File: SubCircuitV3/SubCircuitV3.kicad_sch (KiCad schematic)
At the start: 49 parts, among them J1 JTAG, J10 ESC_POWER, J11 ESC_POWER, J12 ESC_POWER, J13 ESC_POWER, J14 FEMALE XT-60, J15 ESC PWM, J16 5S, J17 Water Sensor Input, J18 3S OUT, J19 2S OUT, J2 ESC PWM, J20 SWITCH, J21 U3V16F15, J22 CAM OUT, J3 ESC PWM, J4 ESC PWM, J5 ESC PWM, J6 ESC PWM, J7 3S, J8 ESC_POWER, J9 ESC_POWER, K1 G5Q-1A, Q1 NMOS, Q2 NMOS, Q3 NMOS, Q4 NMOS, Q5 NMOS, Q6 NMOS

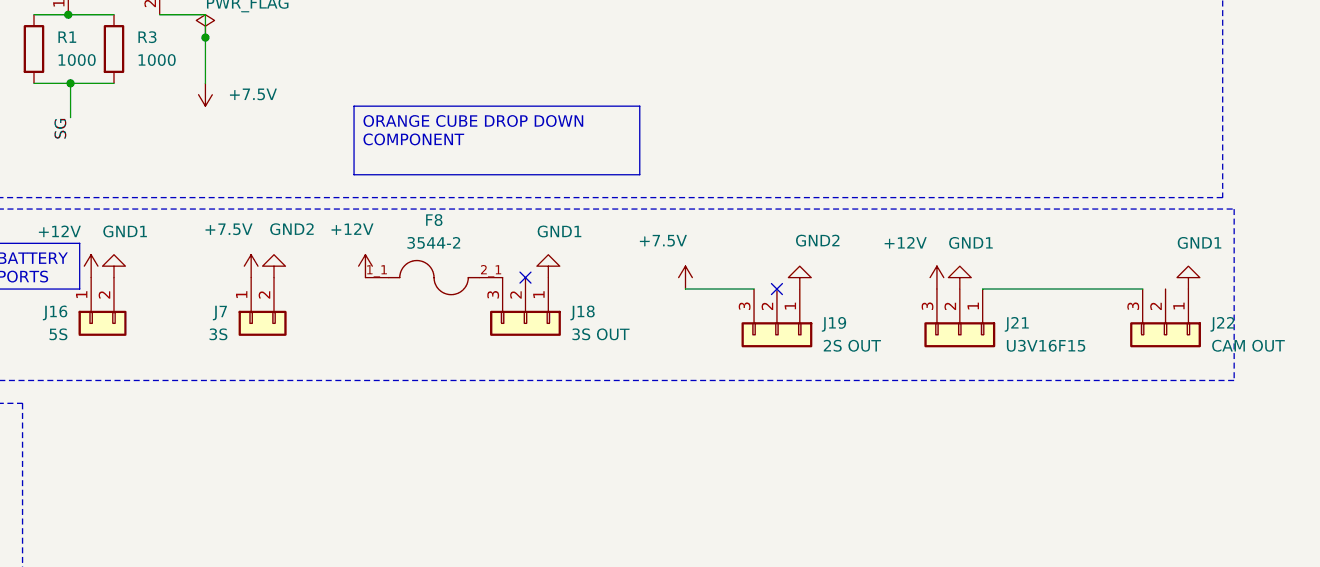
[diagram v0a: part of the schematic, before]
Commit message: Replaced old boost convertor with U3V70F15
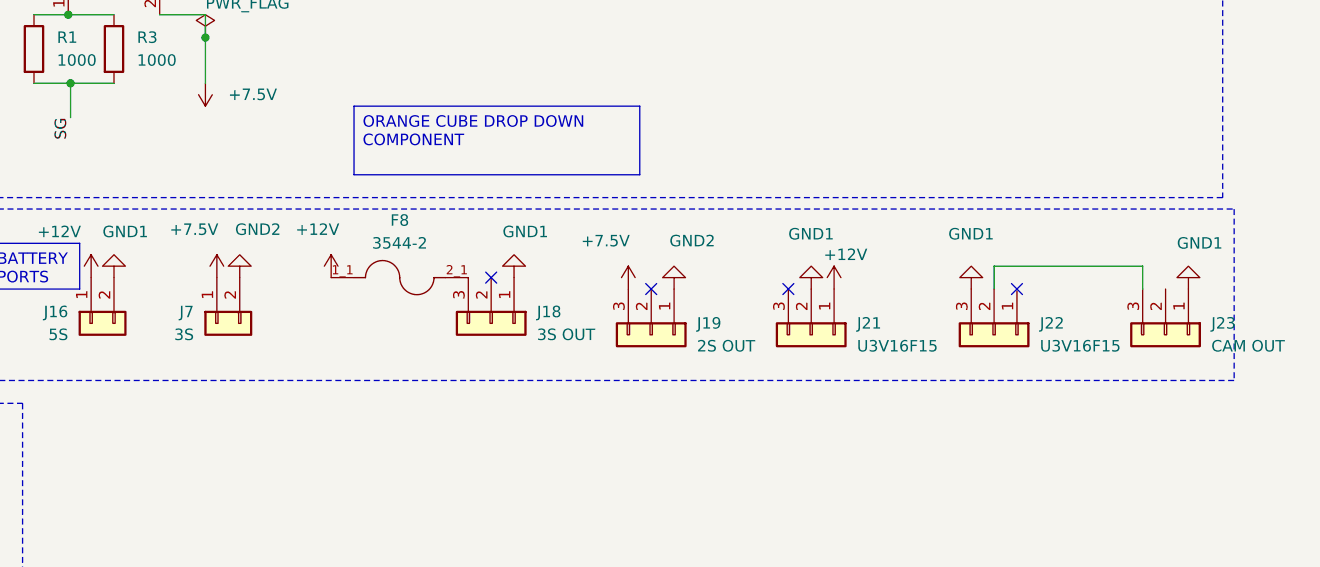
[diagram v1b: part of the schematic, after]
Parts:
- added J21: U3V16F15, Connector_PinHeader_2.54mm:PinHeader_1x03_P2.54mm_Vertical, symbol Connector_Generic:Conn_01x03
- renumbered J21 to J22, J22 to J23
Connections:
- net +12V: now also J21.1 (Pin_1); no longer J22.3 (Pin_3)
- net GND1: now also J22.3 (Pin_3), J21.2 (Pin_2); no longer J22.2 (Pin_2)
- net at J22.1 (Pin_1): no longer J23.3 (Pin_3)
- new net: J22.2 (Pin_2), J23.3 (Pin_3)
- no-connect marks 9 -> 11
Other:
- moved on the sheet: F8, J18, J19, J22, J7

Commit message: Updated WaterSensor pin size
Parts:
- J17: footprint Connector_PinHeader_2.00mm:PinHeader_1x03_P2.00mm_Vertical -> Connector_PinHeader_2.54mm:PinHeader_1x03_P2.54mm_Vertical
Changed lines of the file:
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@@
 			)
 		)
-		(property "Footprint" "Connector_PinHeader_2.00mm:PinHeader_1x03_P2.00mm_Vertical"
+		(property "Footprint" "Connector_PinHeader_2.54mm:PinHeader_1x03_P2.54mm_Vertical"
 			(at 166.37 185.42 0)
 			(effects
